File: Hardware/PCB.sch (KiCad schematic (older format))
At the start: 3 parts

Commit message: Added parts for Ethernet jack and PocketBeagle IO
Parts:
- removed U?: Ag9700, symbol Ag9700
- added BZ?: Buzzer, symbol Buzzer
- added C?: 1000uF, symbol CP1
- added C? (x2): 10uF, symbol C
- added D? (x2): R_LED, symbol LED
- added D? (x2): G_LED, symbol LED
- added P1, P2: Conn_02x18_Odd_Even, symbol Conn_02x18_Odd_Even
- added U?: PN532, symbol PN532
- added U?: Ag9700, symbol Ag9700
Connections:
- net at J?.10 (VC+): now also U?.3 (VB1)
- net at J?.11 (VC-): now also U?.4 (VB2)
- net GND: now reaches J?.13 (SHIELD)
- net GND: now also C?.2, C?.2, C?.2, U?.7 (-VDC)
- net at J?.8 (VC+): now also U?.1 (VA1_RX_in)
- net at J?.9 (VC-): now also U?.2 (VA2_TX_in)
- new net +5V: C?.1, C?.1, C?.1, U?.8 (+VDC)
- no-connect marks 0 -> 3
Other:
- note added: "16v caps\n10uf optional in case of high load\n"
- note added: "IC and SD card facing up"
- note added: "Pocket Beagle IO"
- moved on the sheet: U?

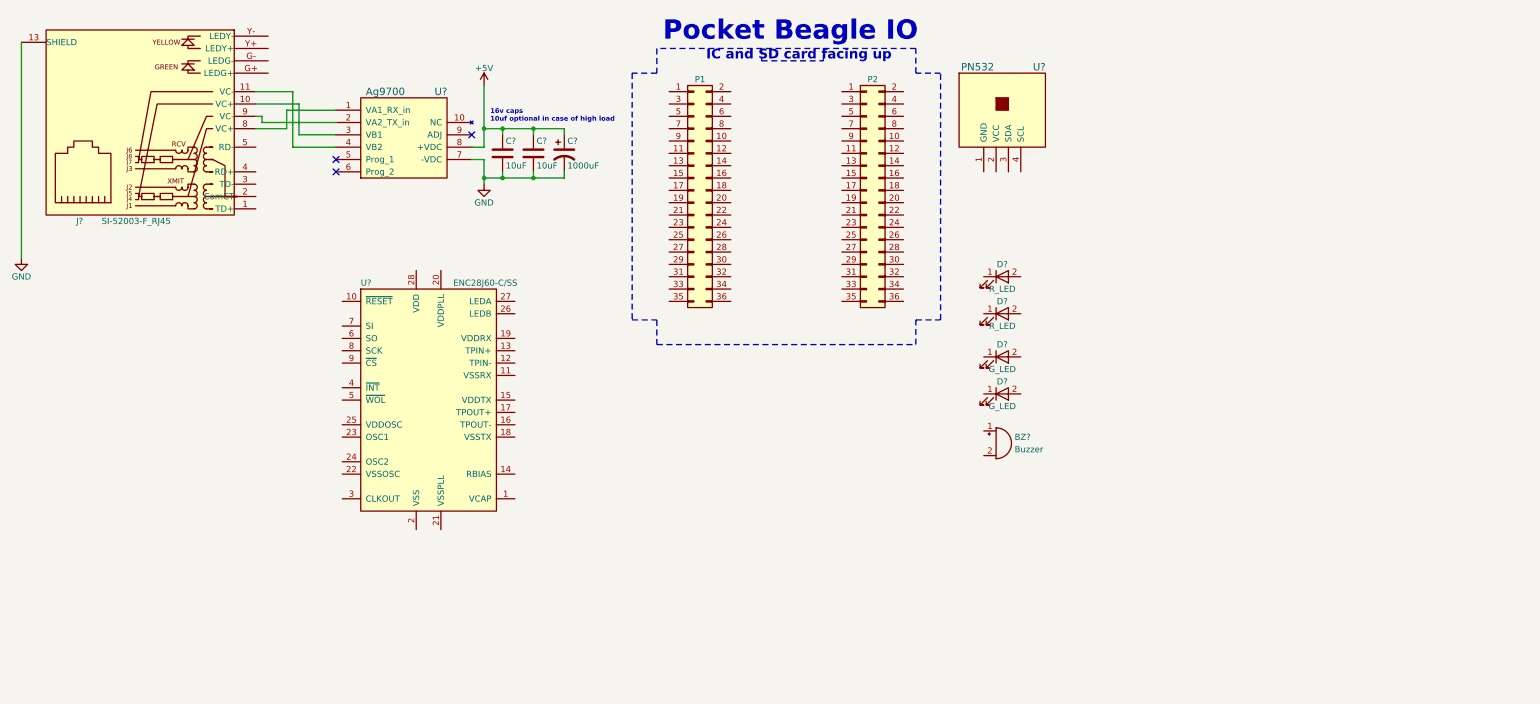
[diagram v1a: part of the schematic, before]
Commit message: Added all parts but motor drive. updated readme parts list
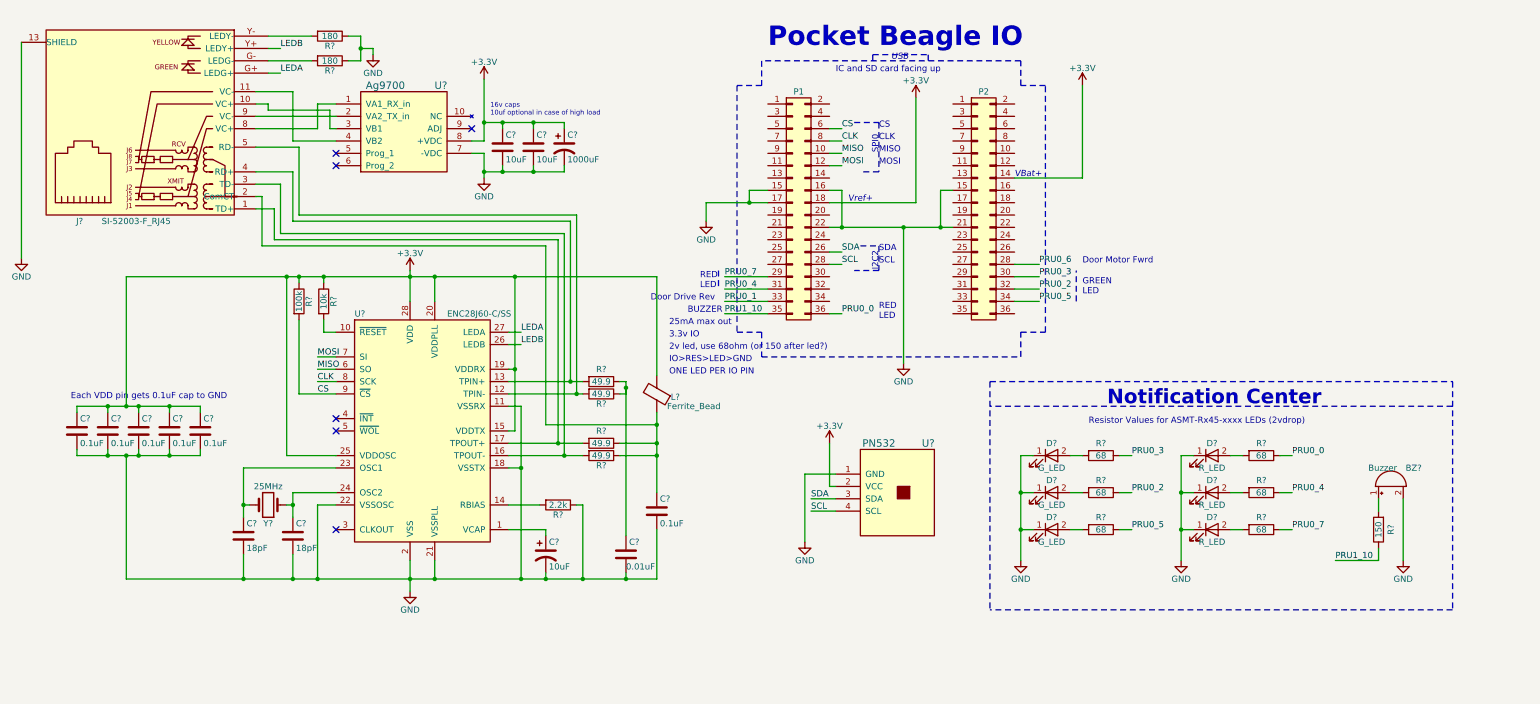
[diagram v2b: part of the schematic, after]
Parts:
- removed D? (x2): G_LED, symbol LED
- added C?: 10uF, symbol CP1
- added C? (x6): 0.1uF, symbol C
- added C? (x2): 18pF, symbol C
- added C?: 0.01uF, symbol C
- added D? (x3): G_LED, symbol LED
- added D?: R_LED, symbol LED
- added L?: Ferrite_Bead, symbol Ferrite_Bead
- added R?: 10k, symbol R
- added R?: 100k, symbol R
- added R?: 2.2k, symbol R
- added R? (x2): 180, symbol R
- added R? (x4): 49.9, symbol R
- added R? (x6): 68, symbol R
- added R?: 150, symbol R
- added Y?: 25MHz, symbol Crystal
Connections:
- net +5V is gone; now on net +3V3: C?.1, C?.1, C?.1, U?.8 (+VDC)
- net GND: now also BZ?.2 (+), D?.1 (K), D?.1 (K), P1.15 (Pin_15), P1.16 (Pin_16), P1.17 (Pin_17), P1.22 (Pin_22), P2.15 (Pin_15), P2.21 (Pin_21), U?.1 (GND), U?.11 (VSSRX), U?.18 (VSSTX), U?.2 (VSS), U?.21 (VSSPLL), U?.22 (VSSOSC), C?.2, C?.2, C?.2, C?.2, C?.2, C?.2, C?.2, C?.2, C?.2, C?.2, D?.1 (K), D?.1 (K), D?.1 (K), D?.1 (K), R?.1, R?.1, R?.1
- net at U?.1 (VCAP): now also C?.1
- net at U?.10 (~RESET): now also R?.2
- net at U?.12 (TPIN-): now also J?.5 (RD-), R?.2
- net at U?.13 (TPIN+): now also J?.4 (RD+), R?.2
- net at U?.14 (RBIAS): now also R?.2
- net +3V3: now reaches U?.15 (VDDTX)
- net +3V3: now also P1.18 (Pin_18), P2.14 (Pin_14), U?.19 (VDDRX), U?.2 (VCC), U?.20 (VDDPLL), U?.25 (VDDOSC), U?.28 (VDD), C?.1, C?.1, C?.1, C?.1, C?.1, L?.2, R?.1, R?.1
- net at U?.16 (TPOUT-): now also J?.3 (TD-), R?.2
- net at U?.17 (TPOUT+): now also J?.1 (TD+), R?.2
- net at U?.23 (OSC1): now also C?.1, Y?.2
- net at U?.24 (OSC2): now also C?.1, Y?.1
- net LEDB: now reaches U?.26 (LEDB)
- net LEDB: now also J?.Y+ (LEDY+)
- net LEDA: now reaches U?.27 (LEDA)
- net LEDA: now also J?.G+ (LEDG+)
- net MISO: now reaches U?.6 (SO)
- net MISO: now also P1.10 (Pin_10)
- net MOSI: now reaches U?.7 (SI)
- net MOSI: now also P1.12 (Pin_12)
- net CLK: now reaches U?.8 (SCK)
- net CLK: now also P1.8 (Pin_8)
- net CS: now reaches U?.9 (~CS)
- net CS: now also P1.6 (Pin_6), R?.2
- net at J?.2 (ComCT): now also C?.1, L?.1, R?.1, R?.1
- net at J?.G- (LEDG-): now also R?.2
- net at J?.Y- (LEDY-): now also R?.2
- net at D?.2 (A): now also R?.2 (x2)
- net at BZ?.1 (-): now also R?.2
- net SDA: now reaches U?.3 (SDA)
- net SDA: now also P1.26 (Pin_26)
- net SCL: now reaches U?.4 (SCL)
- net SCL: now also P1.28 (Pin_28)
- net PRU0_7: now reaches P1.29 (Pin_29)
- net PRU0_7: now also R?.1
- net PRU0_4: now reaches P1.31 (Pin_31)
- net PRU0_4: now also R?.1
- net PRU0_1: now reaches P1.33 (Pin_33)
- net PRU1_10: now reaches P1.35 (Pin_35)
- net PRU1_10: now also R?.1
- net PRU0_0: now reaches P1.36 (Pin_36)
- net PRU0_0: now also R?.1
- net PRU0_6: now reaches P2.28 (Pin_28)
- net PRU0_3: now reaches P2.30 (Pin_30)
- net PRU0_3: now also R?.1
- net PRU0_2: now reaches P2.32 (Pin_32)
- net PRU0_2: now also R?.1
- net PRU0_5: now reaches P2.34 (Pin_34)
- net PRU0_5: now also R?.1
- new net: C?.1, R?.1, R?.1
- new net: D?.2 (A), R?.2 (x4)
- no-connect marks 3 -> 6
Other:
- note added: "25mA max out"
- note added: "2v led, use 68ohm (or 150 after led?)\n"
- note added: "3.3v IO"
- note added: "BUZZER"
- note added: "CLK"
- note added: "CS"
- note added: "Door Drive Rev"
- note added: "Door Motor Fwrd"
- note added: "Each VDD pin gets 0.1uF cap to GND\n"
- note added: "GREEN\nLED"
- note added: "I2C2"
- note added: "IO>RES>LED>GND"
- note added: "MISO"
- note added: "MOSI"
- note added: "Notification Center"
- note added: "ONE LED PER IO PIN"
- note added: "RED\nLED"
- note added: "Resistor Values for ASMT-Rx45-xxxx LEDs (2vdrop)"
- note added: "SCL"
- note added: "SDA"
- note added: "SPI0"
- note added: "USB\n"
- note added: "VBat+"
- note added: "Vref+"
- moved on the sheet: BZ?, C?, D?, P1, P2, U?

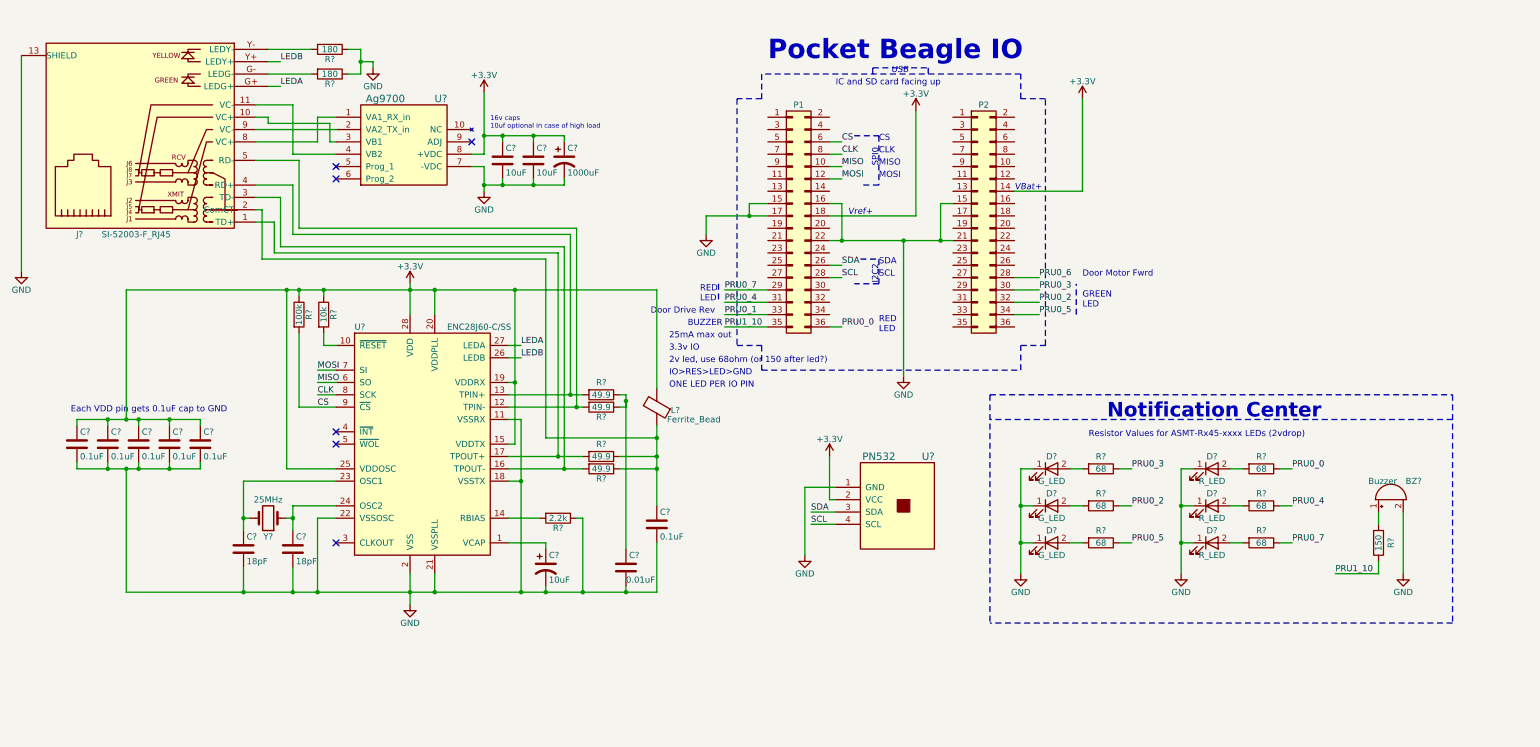
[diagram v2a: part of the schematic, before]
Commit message: added motor driver
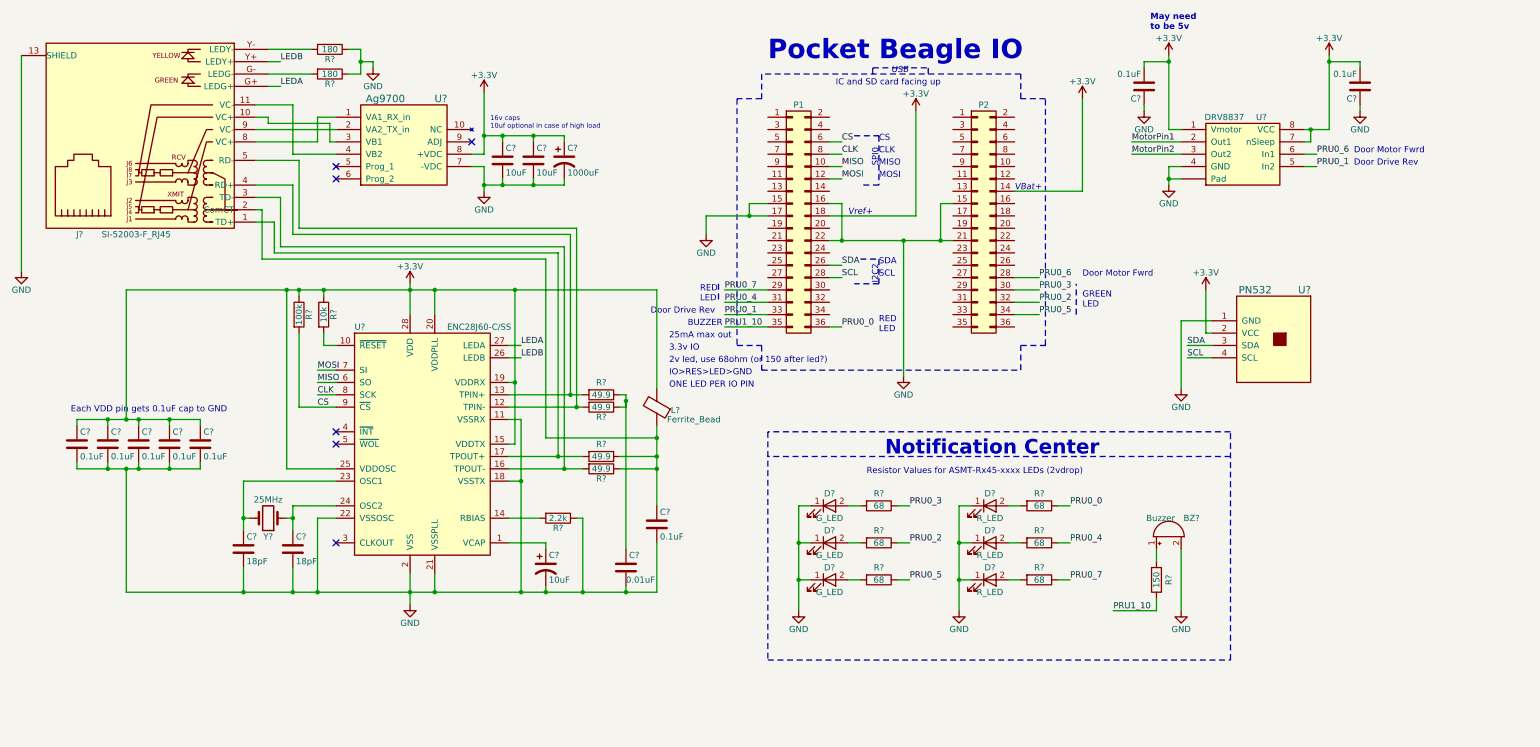
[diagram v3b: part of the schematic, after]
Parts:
- added C? (x2): 0.1uF, symbol C
- added U?: DRV8837, symbol DRV8837
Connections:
- net +3V3: now also C?.2, C?.2, U?.1 (Vmotor), U?.7 (nSleep), U?.8 (VCC)
- net GND: now also C?.1, C?.1, U?.4 (GND), U?.~ (Pad)
- net PRU0_1: now also U?.5 (In2)
- net PRU0_6: now also U?.6 (In1)
- new net MotorPin1: U?.2 (Out1)
- new net MotorPin2: U?.3 (Out2)
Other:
- note added: "May need \nto be 5v"
- moved on the sheet: BZ?, D?, R?, U?

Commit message: cleaned up some of schematic
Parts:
- removed U?: Ag9700, symbol Ag9700
- added C?: 0.1uF, symbol C
- added U?: Ag9700, symbol Ag9700
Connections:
- net +3V3: now also C?.2, U?.8 (+VDC)
- net GND: now also C?.1, U?.7 (-VDC)
- net at J?.10 (VC+): now also U?.3 (VB1)
- net at J?.11 (VC-): now also U?.4 (VB2)
- net at J?.8 (VC+): now also U?.1 (VA1_RX_in)
- net at J?.9 (VC-): now also U?.2 (VA2_TX_in)
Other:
- note added: "Motor Drive"
- note added: "POE Breakout"
- moved on the sheet: BZ?, C?, D?, P1, P2, R?, U?
